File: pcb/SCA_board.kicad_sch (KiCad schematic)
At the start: 60 parts, among them IC1 ST3232BDR, J1 100616-2, J2 39-29-3086, J3 DIN41612_02x32_AC, J4 USB4145-03-0230-C, J5 DE9_Pins, J6 USB4145-03-0230-C, J7 Conn_01x03, U1 USBLC6-2SC6, U2 CH340E, U3 M24C02-WMN

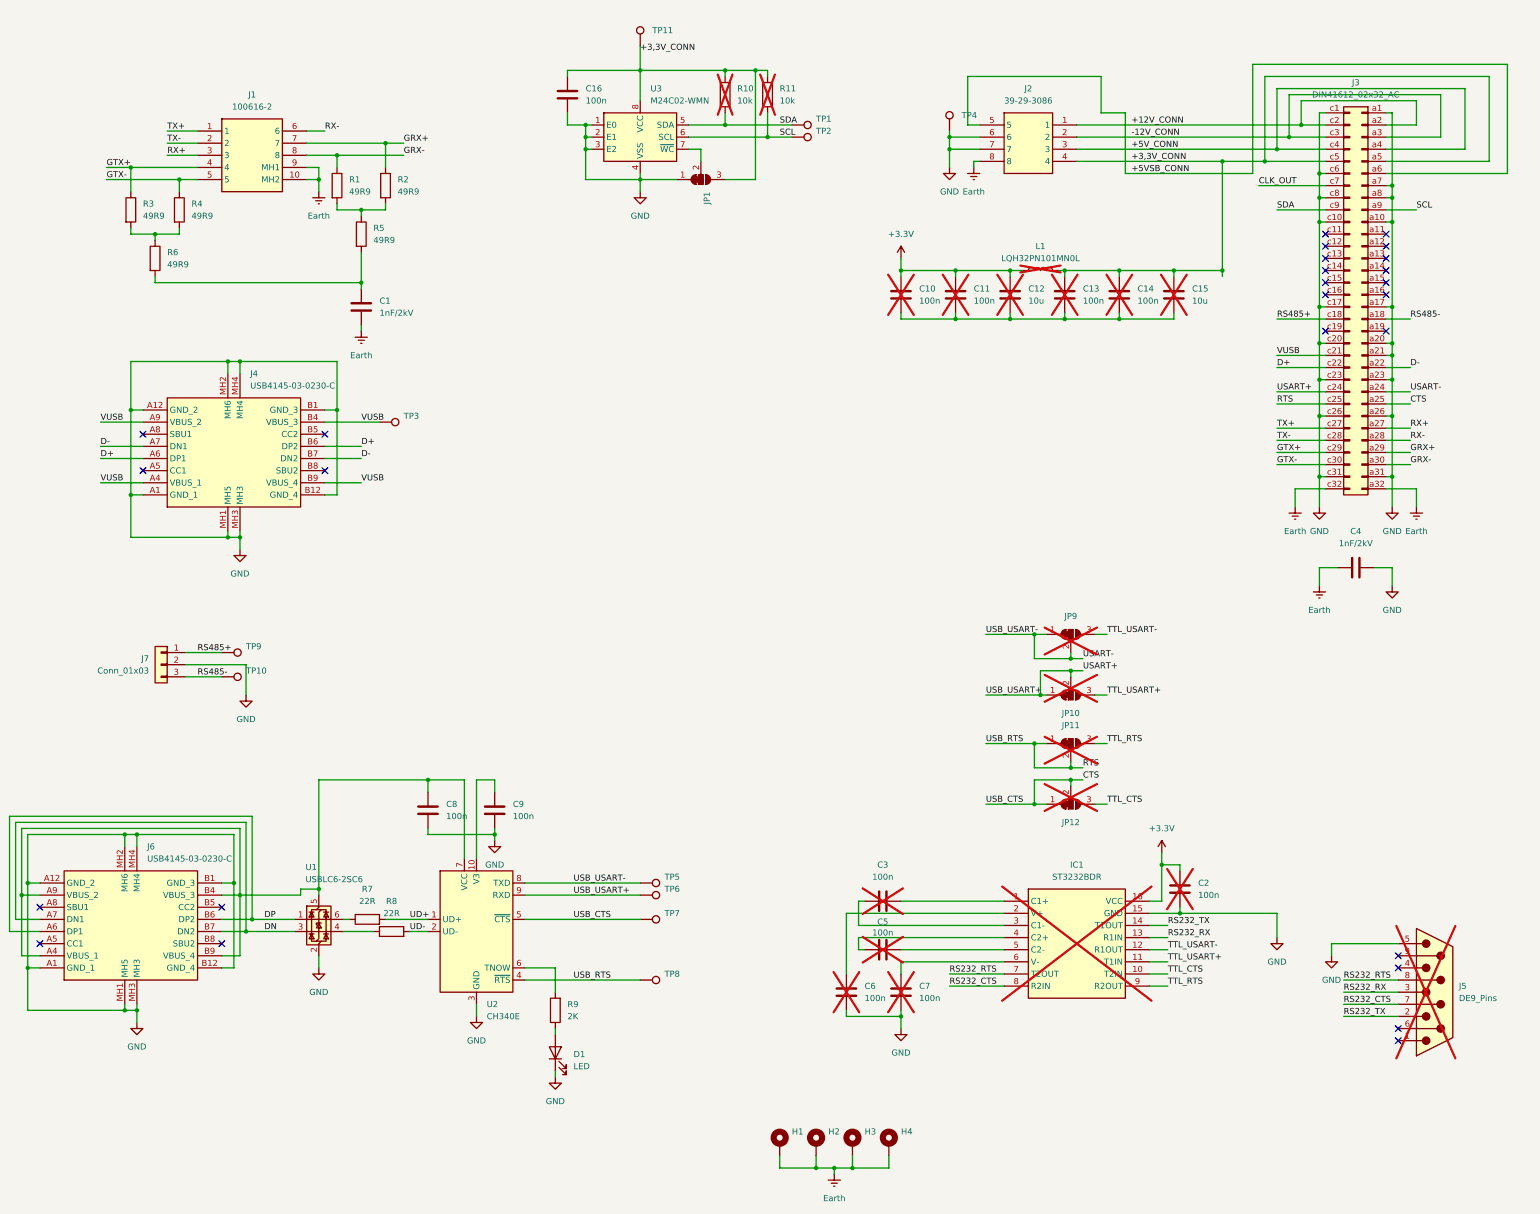
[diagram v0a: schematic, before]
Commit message: Connector and layout change
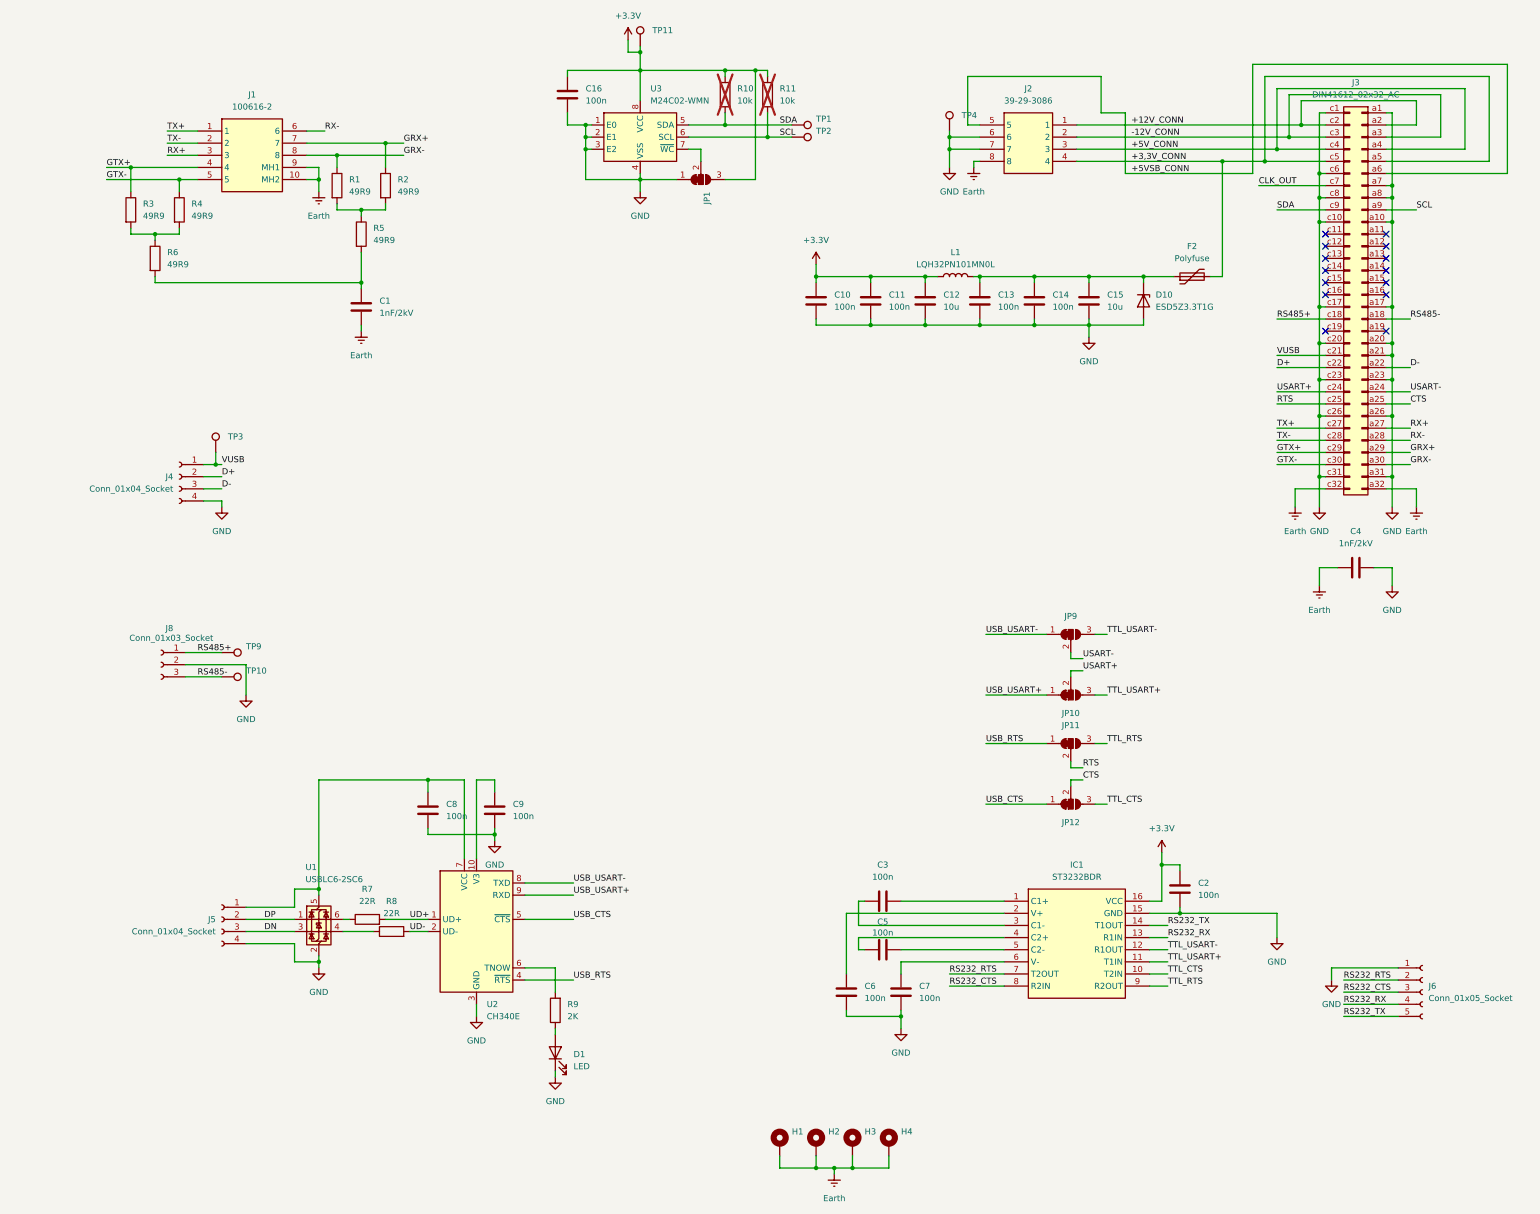
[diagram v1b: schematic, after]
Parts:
- removed J4, J6: USB4145-03-0230-C, SamacSys_Parts:USB4145030230C, symbol SamacSys_Parts:USB4145-03-0230-C
- removed J5: DE9_Pins, Connector_Dsub:DSUB-9_Pins_Vertical_P2.77x2.84mm, symbol Connector:DE9_Pins
- removed J7: Conn_01x03, Connector_Phoenix_MC:PhoenixContact_MCV_1,5_3-G-3.81_1x03_P3.81mm_Vertical, symbol Connector_Generic:Conn_01x03
- removed TP5, TP6, TP7, TP8: TestPoint, TestPoint:TestPoint_Pad_D1.0mm, symbol Connector:TestPoint
- added D10: ESD5Z3.3T1G, Diode_SMD:D_SOD-523, symbol Diode:ESD5Zxx
- added F2: Polyfuse, Fuse:Fuse_1206_3216Metric_Pad1.42x1.75mm_HandSolder, symbol Device:Polyfuse
- added J4, J5: Conn_01x04_Socket, Connector_JST:JST_PH_B4B-PH-K_1x04_P2.00mm_Vertical, symbol Connector:Conn_01x04_Socket
- added J6: Conn_01x05_Socket, Connector_JST:JST_PH_B5B-PH-K_1x05_P2.00mm_Vertical, symbol Connector:Conn_01x05_Socket
- added J8: Conn_01x03_Socket, Connector_JST:JST_PH_B3B-PH-K_1x03_P2.00mm_Vertical, symbol Connector:Conn_01x03_Socket
- C10, C11, C12, C13, C14, C15, C2, C3, C5, C6, C7, L1: now fitted; now in the parts list
- IC1: footprint SOIC127P600X175-16N -> SamacSys_Parts:SOIC127P600X175-16N; now fitted; now in the parts list
- J1: footprint 1006162 -> SamacSys_Parts:1006162
- JP10, JP11, JP12, JP9: now fitted
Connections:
- net +3,3V_CONN: now also F2.2; no longer C13.1, C14.1, C15.1, C16.2, JP1.3 (B), L1.2, R10.2, R11.2, TP11.1, U3.8 (VCC)
- net +3.3V: now also C16.2, JP1.3 (B), R10.2, R11.2, TP11.1, U3.8 (VCC)
- net CTS: no longer JP12.1 (A), U2.5 (~{CTS})
- net D+: now also J4.2 (Pin_2)
- net D-: now also J4.3 (Pin_3)
- net DN: now also J5.3 (Pin_3)
- net DP: now also J5.2 (Pin_2)
- net GND: now also C10.2, C11.2, C12.2, C13.2, C14.2, C15.2, D10.2 (A), J4.4 (Pin_4), J5.4 (Pin_4), J6.1 (Pin_1), J8.2 (Pin_2)
- net RS232_CTS: now also J6.3 (Pin_3)
- net RS232_RTS: now also J6.2 (Pin_2)
- net RS232_RX: now also J6.4 (Pin_4)
- net RS232_TX: now also J6.5 (Pin_5)
- net RS485+: now also J8.1 (Pin_1)
- net RS485-: now also J8.3 (Pin_3)
- net RTS: no longer JP11.1 (A), U2.4 (~{RTS})
- net USART+: no longer JP10.1 (A), U2.9 (RXD)
- net USART-: no longer JP9.1 (A), U2.8 (TXD)
- net VUSB: now also J4.1 (Pin_1)
- net at C8.2, U1.5 (VBUS), U2.7 (VCC): now also J5.1 (Pin_1)
- new net: C13.1, C14.1, C15.1, D10.1 (K), F2.1, L1.2
- new net USB_CTS: JP12.1 (A), U2.5 (~{CTS})
- new net USB_RTS: JP11.1 (A), U2.4 (~{RTS})
- new net USB_USART+: JP10.1 (A), U2.9 (RXD)
- new net USB_USART-: JP9.1 (A), U2.8 (TXD)
- no-connect marks 26 -> 14
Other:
- moved on the sheet: TP3
